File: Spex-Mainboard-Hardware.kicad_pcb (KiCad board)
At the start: 4 copper layers, 100 x 84.7 mm, 124 parts, among them P1 USB_OTG, P13 CONN_01X02, P3 CONN_01X04, P4 CONN_01X04, P5 CONN_01X04, P6 CONN_01X04, P7 CONN_01X02, P8 CONN_01X02, P9 CONN_01X02, Q101 MOS_N_numbered, Q104 MOS_N_numbered, Q105 Si3407DV, Q106 Q_PNP_BEC, Q3 BSS215PH6327, Q4 Si5468DC, Q5 Si5468DC, Q6 Si5468DC, SW1 SW_PUSH, SW2 SW_PUSH, U1 MKL02Z32VFG4, U10 LM4030, U105 TPS563200, U108 TPS563200, U11 MCP2551-I/SN, U12 ST1480ABDR, U13 SCHA4B0419, U14 AT45DB641E, U2 NUP2201MR6, U3 MK20DX256VLH7, U4 NUP2201MR6, U5 NUP2201MR6, U6 MMQA6V2T1G, U7 MCP9808T, U8 BME280, U9 LSM9DS1, Y1 Crystal

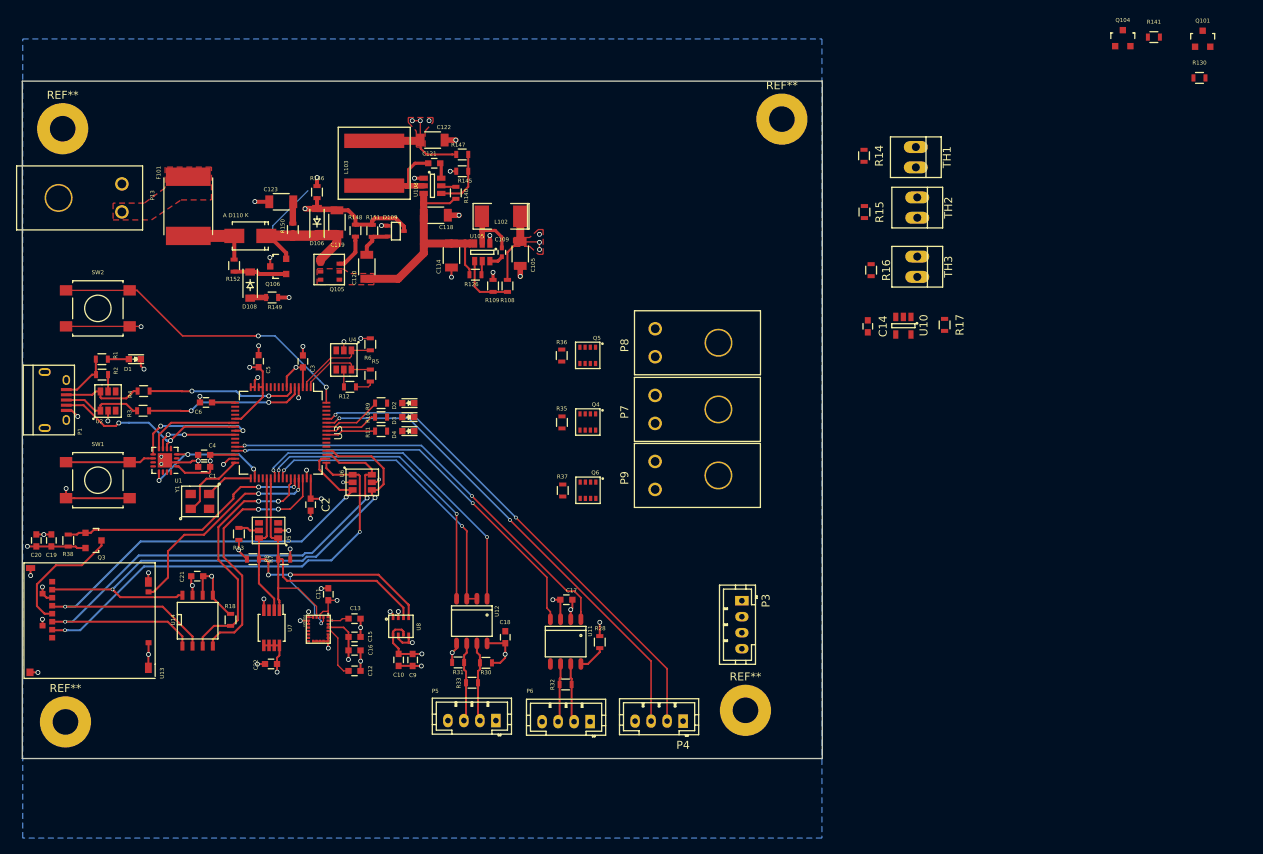
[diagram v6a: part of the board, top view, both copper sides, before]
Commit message: finished routing all but output MOSFETS
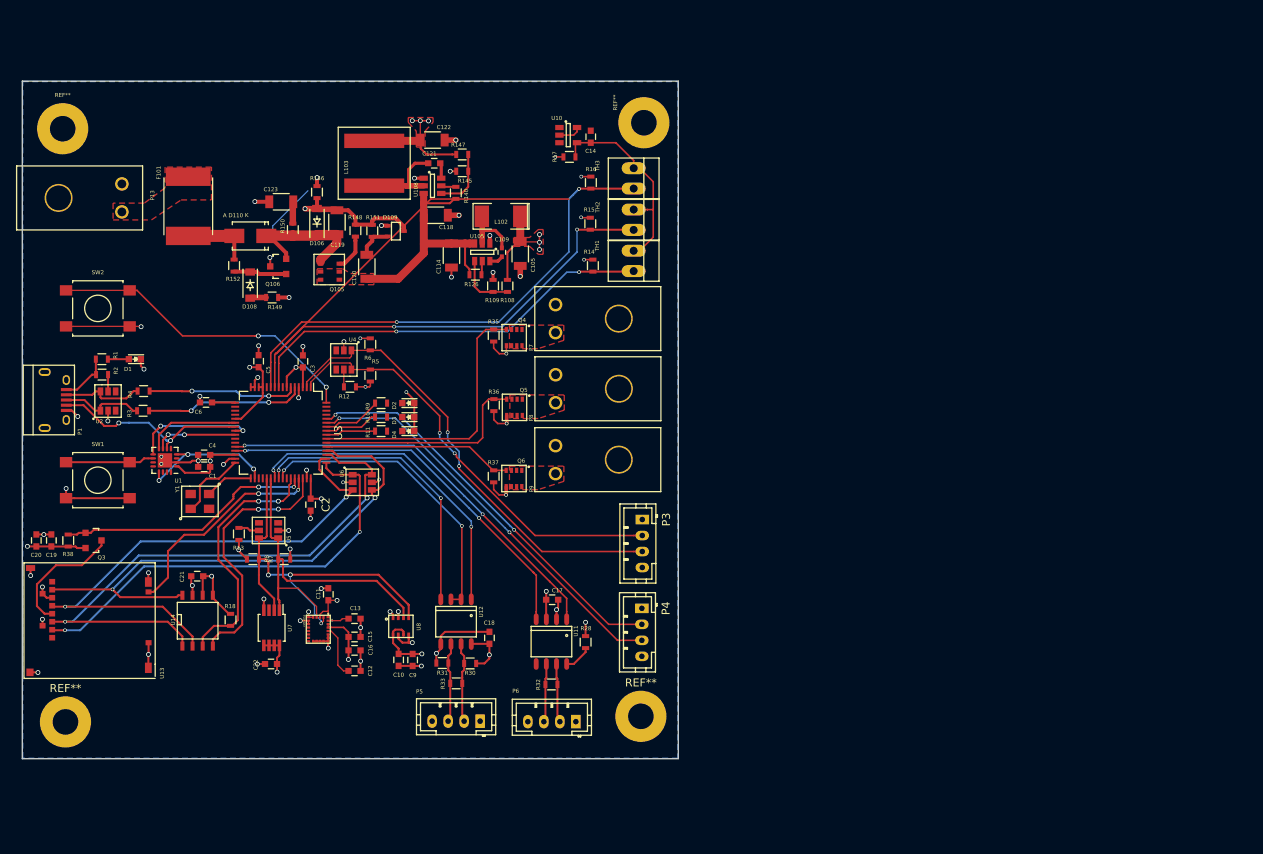
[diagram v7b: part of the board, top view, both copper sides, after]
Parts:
- removed Q101, Q104: MOS_N_numbered, TO_SOT_Packages_SMD:SOT-23
- removed R130, R141: 10K, Resistors_SMD:R_0603
- moved R17 51.4 mm to (84.4, 89.5), turned to 0 degrees
- moved U10 48.2 mm to (84.2, 86.7), turned to 0 degrees
- moved C14 42.0 mm to (87.1, 87.0), turned to 90 degrees
- moved TH1 37.6 mm to (92.4, 102.5)
- moved TH3 37.1 mm to (92.4, 92.2)
- moved R16 36.7 mm to (87.1, 92.7), turned to 90 degrees
- moved R14 36.6 mm to (87.3, 103.1), turned to 90 degrees
- moved TH2 35.5 mm to (92.4, 97.3)
- moved R15 34.3 mm to (87.0, 97.8), turned to 90 degrees
- moved REF** 17.3 mm to (93.7, 85.2)
- moved P7 16.8 mm to (90.6, 109.7)
- moved P3 16.1 mm to (93.5, 134.8)
- moved P4 15.0 mm to (93.5, 145.9), turned to 270 degrees
- moved Q4 14.0 mm to (78.5, 111.0)
- moved R35 13.8 mm to (74.9, 111.8)
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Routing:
- net Temp3: track 0.00 -> 106.6 mm, vias 0 -> 2
- net Temp2: track 0.00 -> 57.2 mm, vias 0 -> 2
- net Temp1: track 0.00 -> 52.6 mm, vias 0 -> 2
- net I2C1_SCL: track 10.7 -> 58.0 mm, vias 0 -> 2
- net I2C1_SDA: track 10.2 -> 54.5 mm, vias 0 -> 2
- net 3.3V_MOS_CTRL: track 0.00 -> 34.9 mm
- net GND: track 103.2 -> 130.7 mm, vias 53 -> 60
- net 5V_MOS_CTRL: track 0.00 -> 27.4 mm
- net /HAB Sensors/2.5VRefVoltage: track 0.00 -> 26.5 mm
- net Vbus_MOS_CTRL: track 0.00 -> 23.7 mm
- net UART2_TX: track 62.7 -> 50.7 mm
- net UART2_RX: track 60.9 -> 51.2 mm
- net Net-(U10-Pad2): track 0.00 -> 2.90 mm
- net +3V3: track 102.9 -> 105.4 mm, vias 19 -> 22
- net CAN0_TX: track 53.9 -> 52.1 mm
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- added copper zone on F.Cu, net /Data_Input_Output/3.3V_MOS_OUT
- added copper zone on F.Cu, net /Data_Input_Output/5V_MOS_OUT
- added copper zone on F.Cu, net /Data_Input_Output/Vbus_MOS_OUT
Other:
- board size 100 x 84.7 mm -> 82 x 84.7 mm

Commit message: updates per week 1 meeting
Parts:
- removed C17: 1uF, Capacitors_SMD:C_0603
- removed R28: 4.7K, Resistors_SMD:R_0603
- removed R32: 120, Resistors_SMD:R_0603
- removed U11: MCP2551-I/SN, Power_Integrations:SO-8
- added P14: CONN_01X02, Connect:PINHEAD1-2, F.Cu at (25.4, 101.9)
- added P2: SWD Header, SPEX_Parts:SWD-10, F.Cu at (37.5, 115.5)
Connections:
- P6 pad 2: /Data_Input_Output/CANH_out -> I/O-1
- P6 pad 3: /Data_Input_Output/CANL_out -> I/O-2
- U3 pad 28: CAN0_TX -> I/O-1
- U3 pad 29: CAN0_RX -> I/O-2
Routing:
- net I/O-1: track 0.00 -> 65.0 mm, vias 0 -> 2
- net I/O-2: track 0.00 -> 63.1 mm, vias 0 -> 2
- net CAN0_TX: track 52.1 -> 0.00 mm, vias 2 -> 0
- net CAN0_RX: track 50.2 -> 0.00 mm, vias 2 -> 0
- net +5V: track 16.1 -> 62.5 mm
- net Temp3: track 106.6 -> 62.0 mm
- net Vbus: track 30.4 -> 64.0 mm, vias 0 -> 1
- net (no net): track 8.24 -> 0.32 mm
- net Net-(C119-Pad2): track 17.8 -> 25.8 mm
- net /Data_Input_Output/CANH_out: track 7.39 -> 0.00 mm
- net /Data_Input_Output/CANL_out: track 7.34 -> 0.00 mm
- net /Toggle: track 39.5 -> 45.3 mm
- net +3V3: track 105.4 -> 101.9 mm, vias 22 -> 21
- net Net-(R28-Pad1): track 3.48 -> 0.00 mm
- net GND: track 130.7 -> 128.9 mm, vias 60 -> 59
